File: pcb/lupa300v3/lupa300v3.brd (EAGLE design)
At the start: 160 x 100 mm, 17 parts

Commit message: more work
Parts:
- added C1, C2, C3, C4, C5, C6: .1uF, rcl:C0603K
- added JP1, JP2: (no value), pinhead:2X08
- added R12, R13, R14, R15, R16, R17, R18, R23: (no value), rcl:R0603
- added R19: 500k, rcl:R0603
- added R20: 1.5M, rcl:R0603
- added R21: 42k, rcl:R0603
- added R22: 110k, rcl:R0603
- moved R11 98.0 mm to (16.3, 43.7)
- moved R10 86.5 mm to (43.4, 27.9), turned to 90 degrees
- moved R9 80.9 mm to (41.1, 27.9), turned to 90 degrees
- moved R8 75.4 mm to (38.9, 27.9), turned to 90 degrees
- moved R7 69.8 mm to (36.6, 27.9), turned to 90 degrees
- moved R6 64.1 mm to (34.0, 27.9), turned to 90 degrees
- moved R5 58.2 mm to (31.0, 27.9), turned to 90 degrees
- moved R4 52.6 mm to (28.4, 27.9), turned to 90 degrees
- moved U$4 49.2 mm to (61.5, 48.5)
- moved R3 47.0 mm to (26.2, 27.9), turned to 90 degrees
- moved R2 41.5 mm to (23.9, 27.9), turned to 90 degrees
- moved R1 35.9 mm to (21.6, 27.9), turned to 90 degrees
- moved U$2 15.2 mm to (49.3, 61.2), turned to 90 degrees
- moved U$5 8.39 mm to (49.0, 56.9), turned to 90 degrees
- moved U$3 6.37 mm to (61.7, 40.6), turned to 90 degrees
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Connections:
- new net ADC_BIAS: C1.1, R12.1, U$1.P$18
- new net BIAS1: C2.1, R19.1, U$1.P$14
- new net BIAS2: C3.1, R20.1, U$1.P$15
- new net BIAS3: C4.1, R21.1, U$1.P$16
- new net BIAS4: C5.1, R22.1, U$1.P$17
- new net N$27: U$1.P$41
- new net N$28: U$1.P$42
- new net N$29: U$2.2
- new net N$30: U$2.1
- new net N$58: JP1.1
- new net N$59: JP1.3
- new net N$60: JP1.5
- new net N$61: JP1.7
- new net N$62: JP1.9
- new net N$63: JP1.11
- new net N$64: JP1.13
- new net N$65: JP1.15
- new net N$66: JP1.2
- new net N$67: JP1.4
- new net N$68: JP1.6
- new net N$69: JP1.8
- new net N$70: JP1.10
- new net N$71: JP1.12
- new net N$72: JP1.14
- new net N$73: JP1.16
- new net N$74: JP2.1
- new net N$75: JP2.3
- new net N$76: JP2.5
- new net N$77: JP2.7
- new net N$78: JP2.9
- new net N$79: JP2.11
- new net N$80: JP2.13
- new net N$81: JP2.15
- new net N$82: JP2.2
- new net N$83: JP2.4
- new net N$84: JP2.6
- new net N$85: JP2.8
- new net N$86: JP2.10
- new net N$87: JP2.12
- new net N$88: JP2.14
- new net N$89: JP2.16
- new net PRE_BIAS: C6.1, R23.1, U$1.P$40
- net GNDA: now also C2.2, C3.2, C4.2, C5.2
- net GNDADC: now also C1.2
- net GND_PIX: now also C6.2
- net INT1: now also R18.1
- net INT2: now also R17.1
- net N$21: now also R13.1
- net N$23: now also R14.1
- net N$24: now also R15.1
- net N$25: now also R16.1
- net VADC: now also R12.2
- net VDDA: now also R19.2, R20.2, R21.2, R22.2
- net VPIX: now also R23.2
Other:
- board size 160 x 100 mm -> 69.8 x 100 mm

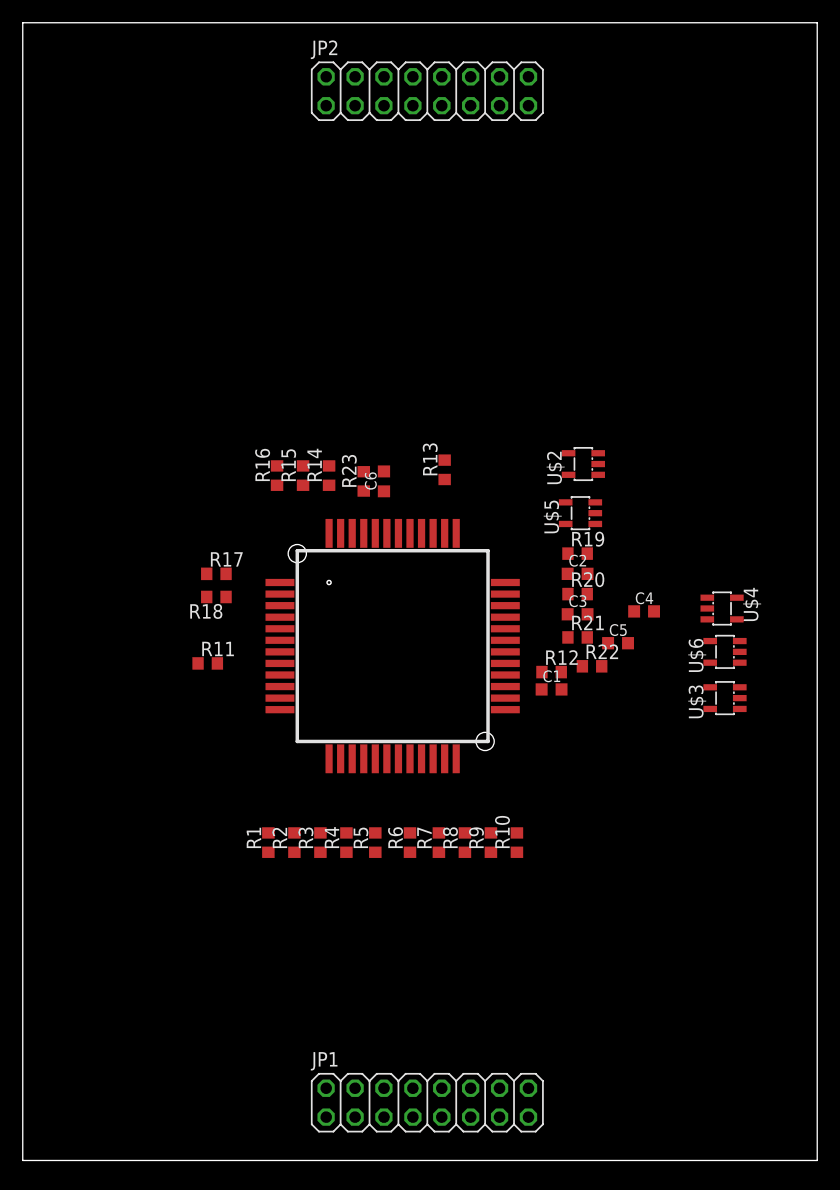
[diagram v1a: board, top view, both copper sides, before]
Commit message: added adc output buffer
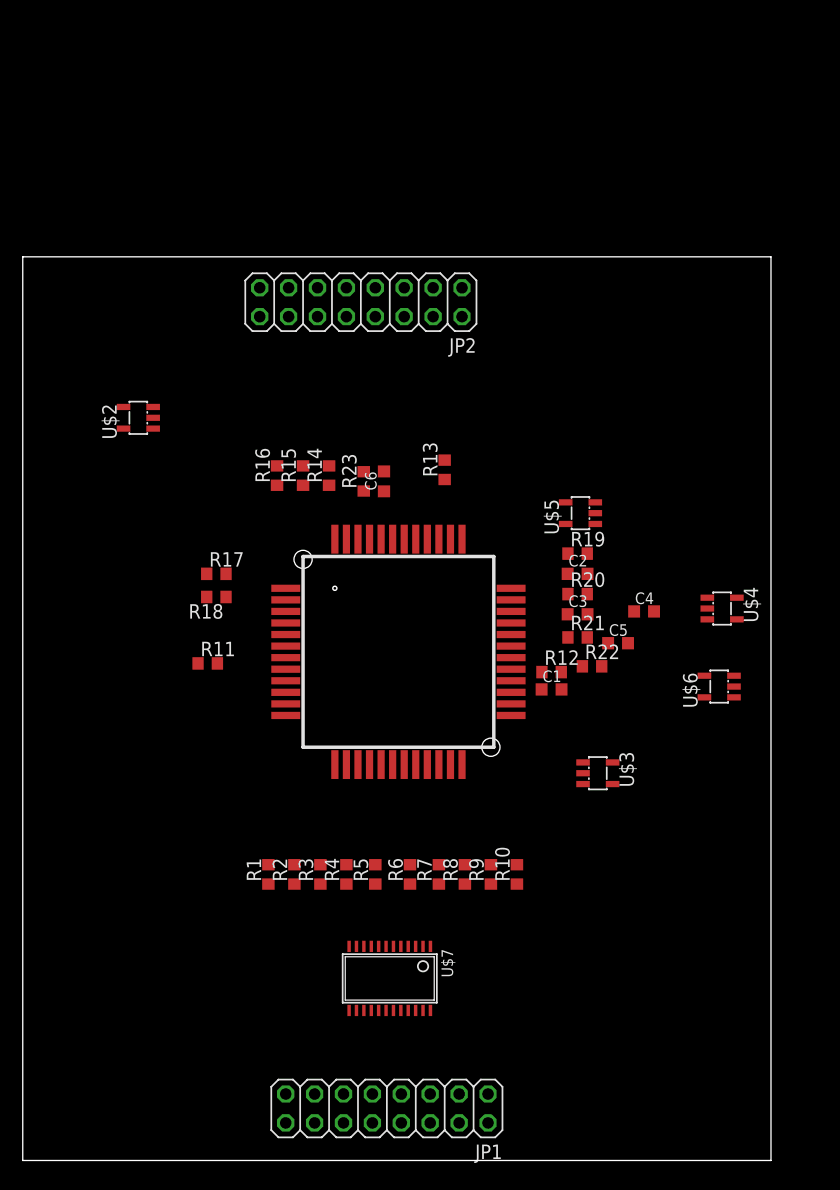
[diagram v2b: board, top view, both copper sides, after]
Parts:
- added U$7: 74LVC827A, lupa300-components:TSSOP24
- moved U$2 39.3 mm to (10.2, 65.3)
- moved JP2 19.4 mm to (29.7, 75.4), turned to 180 degrees
- moved U$3 13.0 mm to (50.5, 34.0), turned to 270 degrees
- moved JP1 3.59 mm to (32.0, 4.57), turned to 180 degrees
- moved U$6 3.09 mm to (61.2, 41.7)
- moved R1 2.79 mm to (21.6, 25.1)
- moved R10 2.79 mm to (43.4, 25.1)
- moved R2 2.79 mm to (23.9, 25.1)
- moved R3 2.79 mm to (26.2, 25.1)
- moved R4 2.79 mm to (28.4, 25.1)
- moved R5 2.79 mm to (31.0, 25.1)
- moved R6 2.79 mm to (34.0, 25.1)
- moved R7 2.79 mm to (36.6, 25.1)
- moved R8 2.79 mm to (38.9, 25.1)
- moved R9 2.79 mm to (41.1, 25.1)
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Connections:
- net N$20 renamed SPI_EN
- net N$22 renamed SPI_DATA
- removed net N$10 (its old number): U$4.3
- removed net N$11 (its old number): U$6.1
- removed net N$12 (its old number): U$6.3
- removed net N$3 (its old number): U$5.3
- removed net N$30: U$2.1
- removed net N$4 (its old number): U$5.1
- removed net N$58: JP1.1
- removed net N$59: JP1.3
- removed net N$6 (its old number): U$3.3
- removed net N$60: JP1.5
- removed net N$61: JP1.7
- removed net N$62: JP1.9
- removed net N$63: JP1.11
- removed net N$64: JP1.13
- removed net N$65: JP1.15
- removed net N$66: JP1.2
- removed net N$67: JP1.4
- removed net N$68: JP1.6
- removed net N$69: JP1.8
- removed net N$7 (its old number): U$3.1
- removed net N$70: JP1.10
- removed net N$71: JP1.12
- removed net N$72: JP1.14
- removed net N$73: JP1.16
- removed net N$8 (its old number): U$4.1
- removed net N$81: JP2.15
- removed net N$89: JP2.16
- new net 5V: JP2.15, JP2.16, U$2.1, U$3.1, U$4.1, U$5.1, U$6.1
- new net ENABLE: U$2.3, U$3.3, U$4.3, U$5.3, U$6.3
- new net FRAME_VALID: R15.2
- new net GND: JP1.1, JP1.2
- new net INT_TIME1: R18.2
- new net INT_TIME2: R17.2
- new net INT_TIME3: R16.2
- new net LINE_VALID: R14.2
- new net N$26: R10.1, U$7.2
- new net N$31: R9.1, U$7.3
- new net N$32: R8.1, U$7.4
- new net N$33: R7.1, U$7.5
- new net N$34: R6.1, U$7.6
- new net N$35: R5.1, U$7.7
- new net N$36: R4.1, U$7.8
- new net N$37: R3.1, U$7.9
- new net N$38: R2.1, U$7.10
- new net N$39: R1.1, U$7.11
- new net SPI_CLK: R13.2
- net CLK: now also JP1.15
- net D0: now also JP1.12, U$7.14; no longer R1.1
- net D1: now also JP1.11, U$7.15; no longer R2.1
- net D2: now also JP1.10, U$7.16; no longer R3.1
- net D3: now also JP1.9, U$7.17; no longer R4.1
- net D4: now also JP1.8, U$7.18; no longer R5.1
- net D5: now also JP1.7, U$7.19; no longer R6.1
- net D6: now also JP1.6, U$7.20; no longer R7.1
- net D7: now also JP1.5, U$7.21; no longer R8.1
- net D8: now also JP1.4, U$7.22; no longer R9.1
- net D9: now also JP1.3, U$7.23; no longer R10.1
- net GNDD: now also U$7.12
- net RESET: now also JP1.16
- net VDD: now also U$7.24
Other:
- board size 69.8 x 100 mm -> 65.8 x 79.4 mm

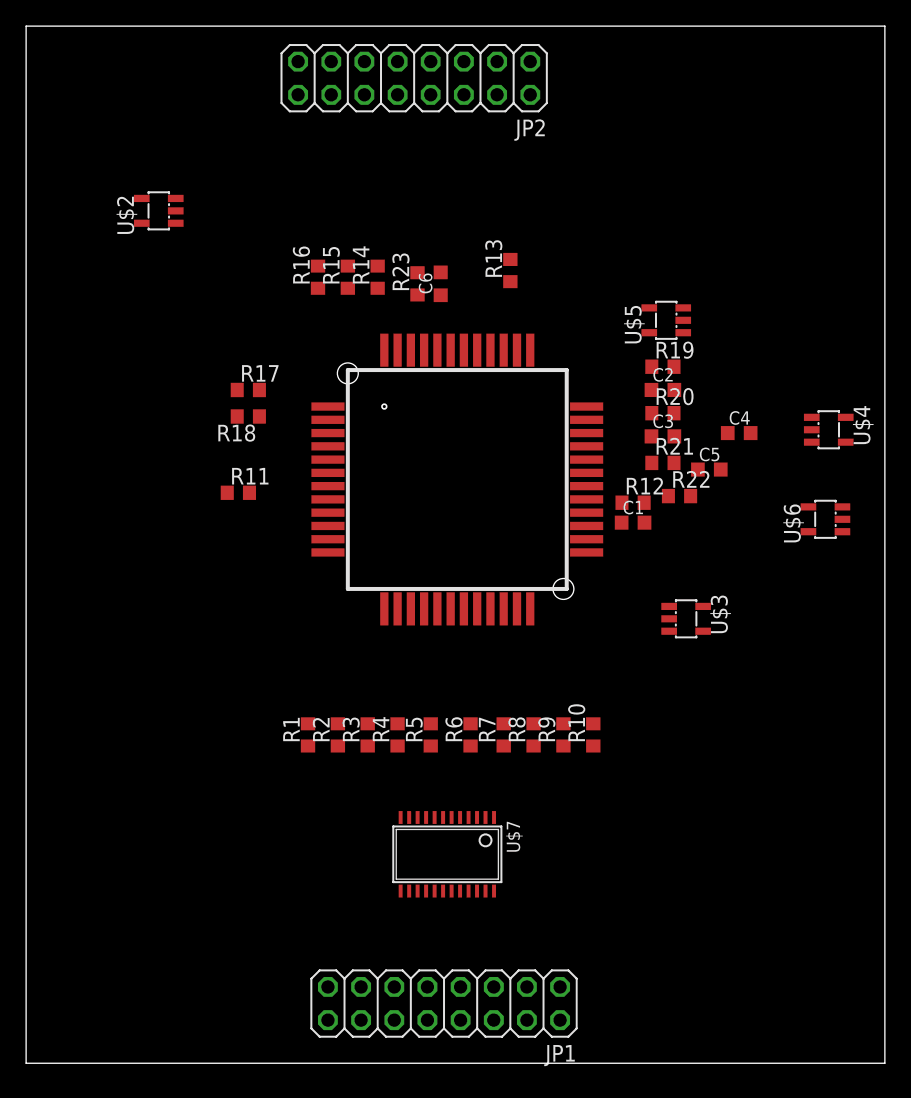
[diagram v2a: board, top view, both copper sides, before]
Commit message: added separate ground planes
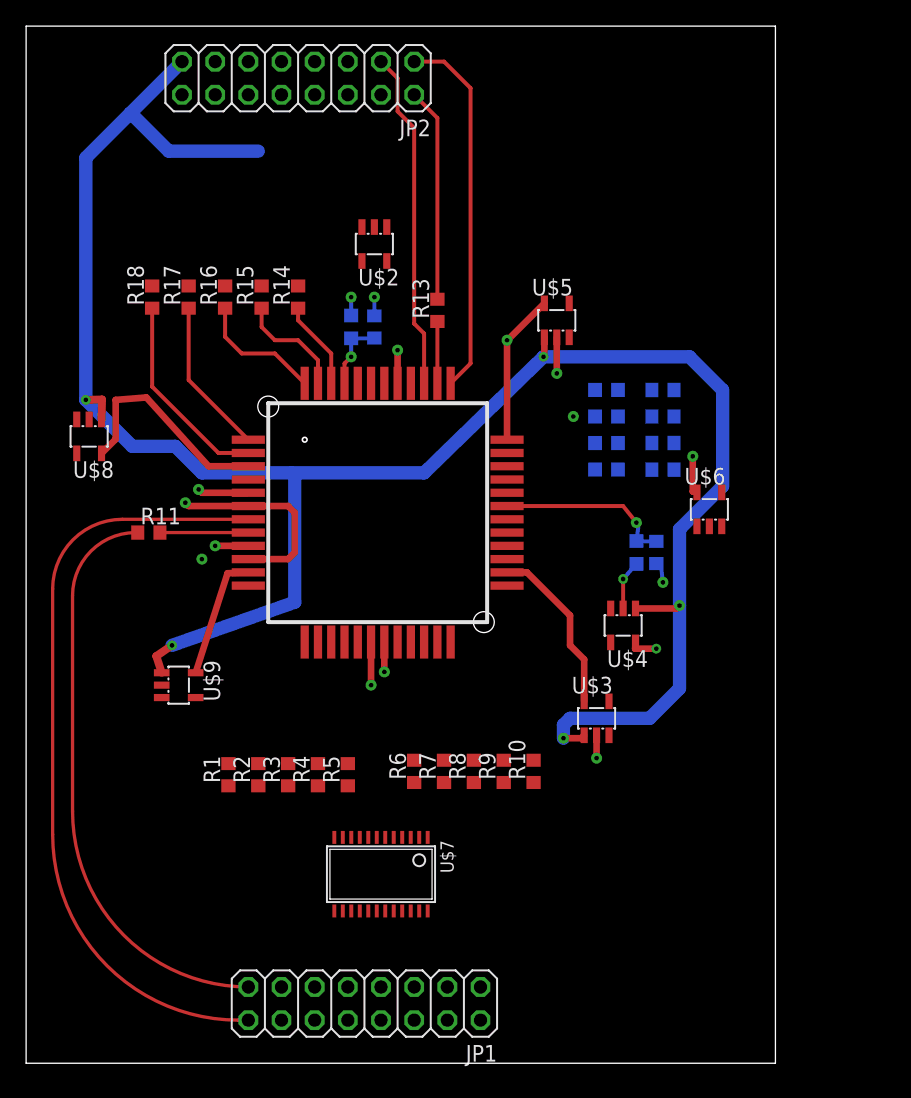
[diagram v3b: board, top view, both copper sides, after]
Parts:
- added U$8, U$9: XC6210B252MR-G, lupa300-components:SOT25
- moved U$4 21.7 mm to (45.7, 33.5), turned to 180 degrees
- moved U$2 16.7 mm to (26.7, 62.7), turned to 180 degrees
- moved R18 11.7 mm to (9.65, 58.7), turned to 90 degrees
- moved U$3 10.3 mm to (43.7, 26.4), turned to 0 degrees
- moved C4 10.2 mm to (44.5, 47.5), flipped to the bottom
- moved U$6 8.92 mm to (52.3, 42.4), turned to 0 degrees
- moved JP2 8.89 mm to (20.8, 75.4)
- moved R17 8.45 mm to (12.4, 58.7), turned to 90 degrees
- moved U$5 8.38 mm to (40.6, 56.9), turned to 0 degrees
- moved C5 7.87 mm to (44.5, 45.5), flipped to the bottom
- moved C6 7.61 mm to (24.9, 56.4), flipped to the bottom
- moved R11 7.50 mm to (9.40, 40.6)
- moved R16 7.27 mm to (15.2, 58.7)
- moved R5 7.04 mm to (24.6, 22.1)
- moved R1 6.82 mm to (15.5, 22.1)
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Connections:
- removed net N$74: JP2.1
- removed net N$75: JP2.3
- removed net N$82: JP2.2
- new net N$40: U$8.3
- new net VDDD1: U$1.P$10, U$8.5
- new net VDDO: U$1.P$2, U$9.5
- net 5V: now also U$8.1, U$9.1
- net GNDD: now also U$8.2, U$9.2
- net SPI_CLK: now also JP2.2
- net SPI_DATA: now also JP2.3
- net SPI_EN: now also JP2.1
- net VDD: no longer U$1.P$10, U$1.P$2
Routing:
- net 5V: track 0.00 -> 163.2 mm, vias 0 -> 5
- net RESET: track 0.00 -> 56.9 mm
- net CLK: track 0.00 -> 42.5 mm
- net SPI_EN: track 0.00 -> 28.4 mm
- net SPI_DATA: track 0.00 -> 26.0 mm
- net VDDD1: track 0.00 -> 17.0 mm
- net SPI_CLK: track 0.00 -> 16.4 mm
- net GNDA: track 0.00 -> 15.5 mm, vias 0 -> 2
- net INT1: track 0.00 -> 15.5 mm
- net ADC_BIAS: track 0.00 -> 13.9 mm, vias 0 -> 1
- net VDD: track 0.00 -> 13.2 mm
- net VPIX: track 0.00 -> 13.1 mm, vias 0 -> 2
- net INT2: track 0.00 -> 12.0 mm
- net N$25: track 0.00 -> 9.77 mm
- net VADC: track 0.00 -> 9.73 mm, vias 0 -> 4
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- added copper zone on layer 2, net GNDA
- added copper zone on layer 2, net GNDADC
- added copper zone on layer 2, net GNDD
- added copper zone on layer 2, net GND_PIX
- added copper zone on layer 15, net VADC
- added copper zone on layer 15, net VDDA
- added copper zone on layer 15, net VPIX
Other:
- board size 65.8 x 79.4 mm -> 57.4 x 79.4 mm
